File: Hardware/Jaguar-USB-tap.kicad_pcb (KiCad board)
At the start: 2 copper layers, 40 x 70 mm, 24 parts, among them J1 DB15, P1 CONN_01X03, P2 USB_B, P3 CONN_01X05, U1 NCP1117ST33T3G, U2 STM32F070F6, U3 TXB0106, U4 TXB0106, Y1 8MHz

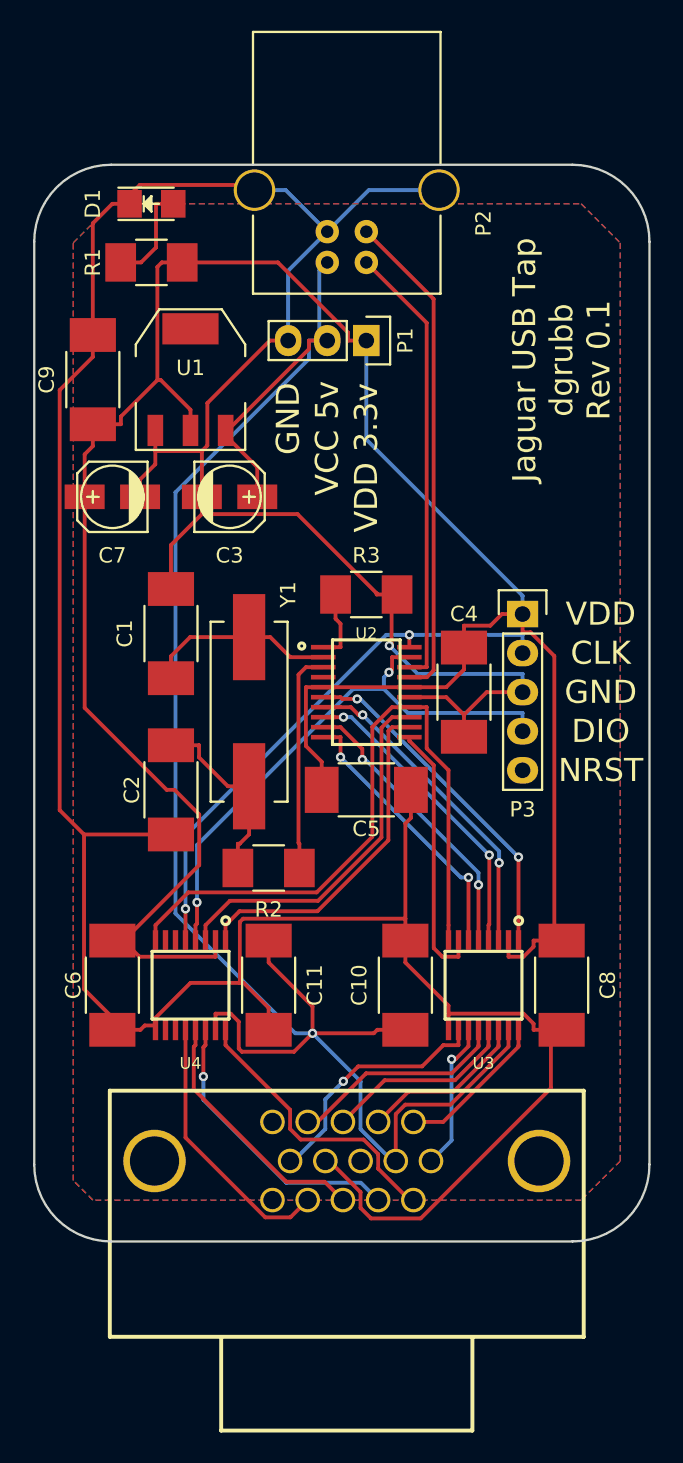
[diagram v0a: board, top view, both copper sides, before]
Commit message: Circuit improvements.
1) Add an indicator LED to OE.
2) Add a capacitor to NRST.
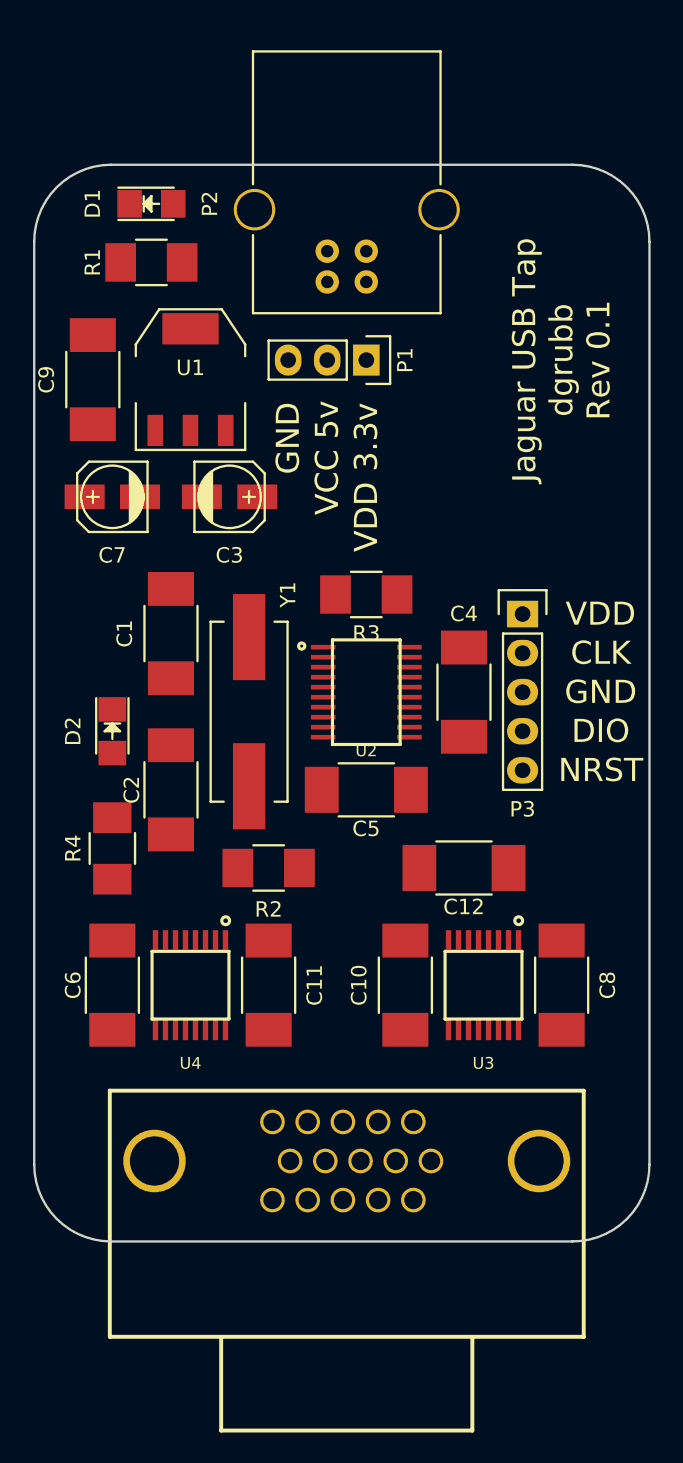
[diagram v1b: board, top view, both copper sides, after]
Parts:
- added C12: 0.1uF, Capacitors_SMD:C_1812_HandSoldering, F.Cu at (144.8, 90.2)
- added D2: LED, LEDs:LED_1206, F.Cu at (121.9, 81.3)
- added R4: 650, Resistors_SMD:R_1210_HandSoldering, F.Cu at (121.9, 88.9)
- moved P2 1.27 mm to (135.9, 52.1)
- moved P1 1.27 mm to (138.4, 57.1)
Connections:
- U2 pad 5: VDD -> NRST
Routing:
- net GNDREF: track 239.8 -> 0.00 mm, vias 1 -> 0
- net VDD: track 155.2 -> 0.00 mm
- net VCC: track 121.1 -> 0.00 mm, vias 1 -> 0
- net OE: track 44.5 -> 0.00 mm
- net R5_VDD: track 36.9 -> 0.00 mm, vias 2 -> 0
- net R6_VDD: track 36.2 -> 0.00 mm, vias 2 -> 0
- net D-: track 32.1 -> 0.00 mm
- net D+: track 29.1 -> 0.00 mm
- net R4_VDD: track 24.1 -> 0.00 mm
- net R3_VDD: track 22.5 -> 0.00 mm
- net C1_VDD: track 22.5 -> 0.00 mm, vias 2 -> 0
- net C2_VDD: track 21.2 -> 0.00 mm, vias 2 -> 0
- net C3_VDD: track 20.1 -> 0.00 mm, vias 2 -> 0
- net C4_VDD: track 18.9 -> 0.00 mm, vias 2 -> 0
- net R4_VCC: track 18.7 -> 0.00 mm, vias 1 -> 0
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- removed copper zone on B.Cu, net GNDREF
- removed copper zone on F.Cu, net VDD

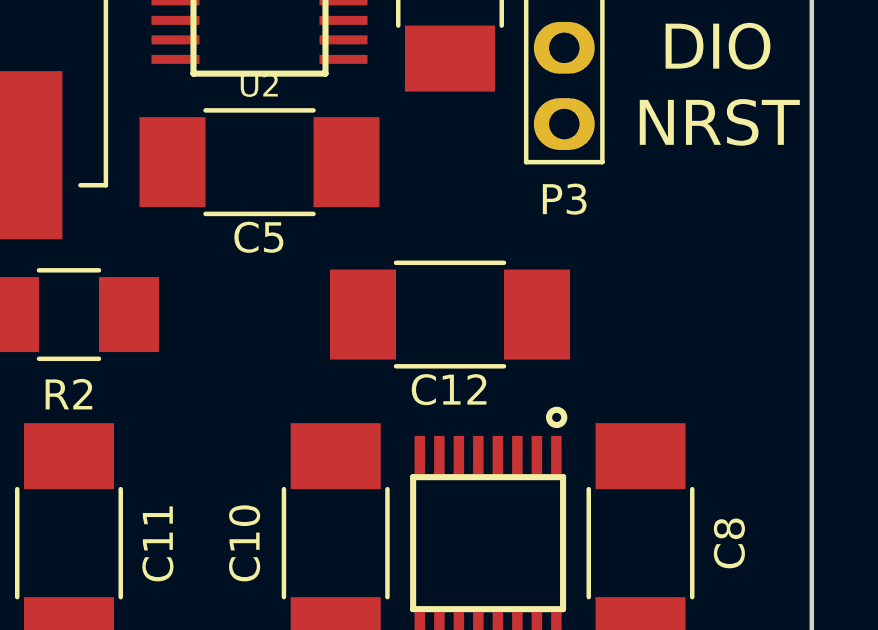
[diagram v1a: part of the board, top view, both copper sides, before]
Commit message: Minor tweaks for PCB layout positioning of components.
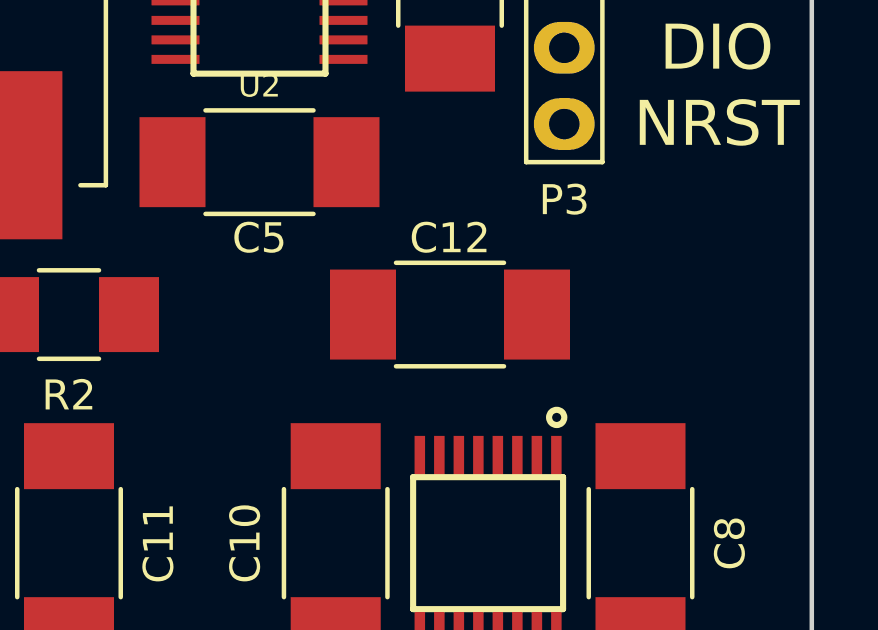
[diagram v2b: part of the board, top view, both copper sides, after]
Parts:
- turned C12 to 180 degrees
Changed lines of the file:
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@@
   )
   (module Capacitors_SMD:C_1812_HandSoldering (layer F.Cu)
-    (at 144.78 90.17)
+    (at 144.78 90.17 180)
     (descr "Capacitor SMD 1812, hand soldering")
     (tags "capacitor 1812")
     (attr smd)
-    (fp_text reference C12 (at 0 2.54) (layer F.SilkS)
+    (fp_text reference C12 (at 0 2.54 180) (layer F.SilkS)
       (effects (font (size 1 1) (thickness 0.15)))
     )
-    (fp_text value 0.1uF (at 0 3) (layer F.Fab)
+    (fp_text value 0.1uF (at 0 3 180) (layer F.Fab)
       (effects (font (size 1 1) (thickness 0.15)))
     )
@@
     (fp_line (start 1.8 -1.725) (end -1.8 -1.725) (layer F.SilkS) (width 0.15))
     (fp_line (start -1.8 1.725) (end 1.8 1.725) (layer F.SilkS) (width 0.15))
-    (pad 1 smd rect (at -2.9 0) (size 2.2 3) (layers F.Cu F.Paste F.Mask)
+    (pad 1 smd rect (at -2.9 0 180) (size 2.2 3) (layers F.Cu F.Paste F.Mask)
       (net 24 NRST))
-    (pad 2 smd rect (at 2.9 0) (size 2.2 3) (layers F.Cu F.Paste F.Mask)
+    (pad 2 smd rect (at 2.9 0 180) (size 2.2 3) (layers F.Cu F.Paste F.Mask)
       (net 2 GNDREF))
     (model Capacitors_SMD.3dshapes/C_1812_HandSoldering.wrl

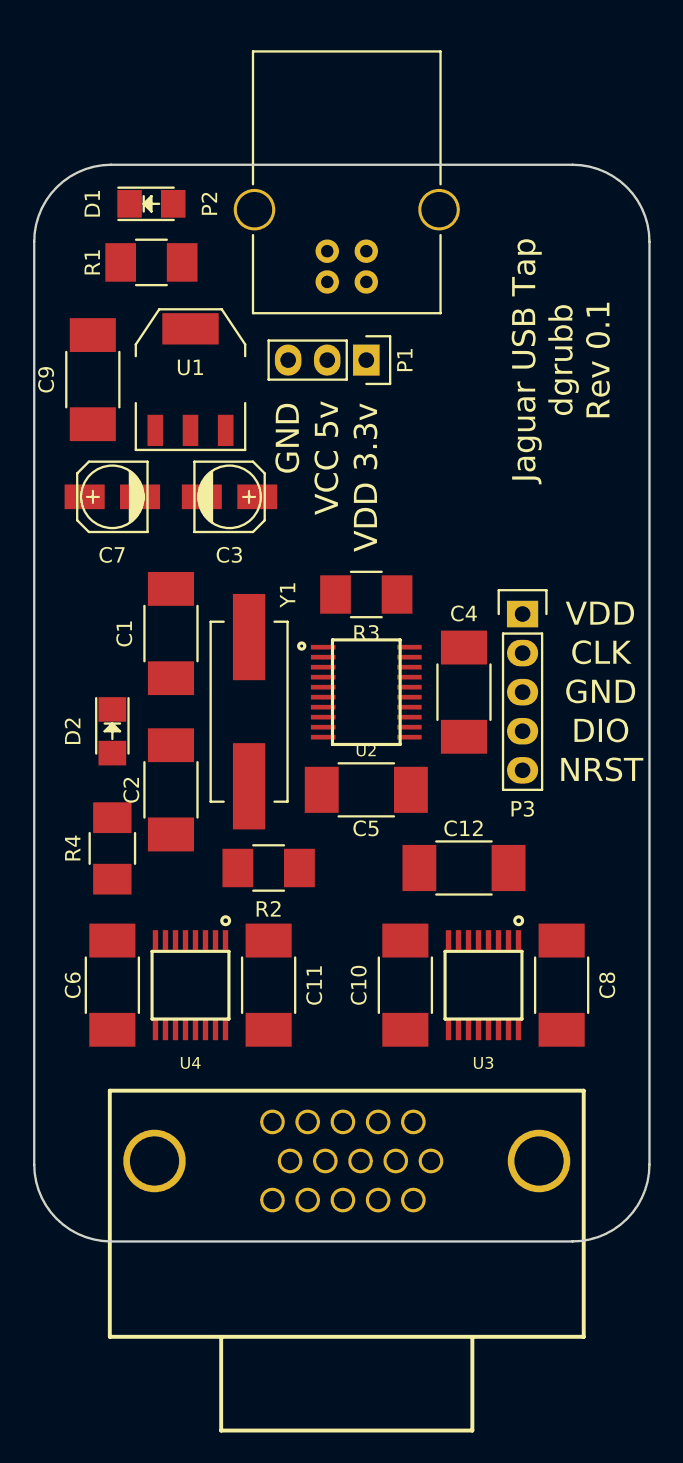
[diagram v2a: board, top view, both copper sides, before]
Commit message: Update Gerbers and drill files to reflect tweaks to schematic.
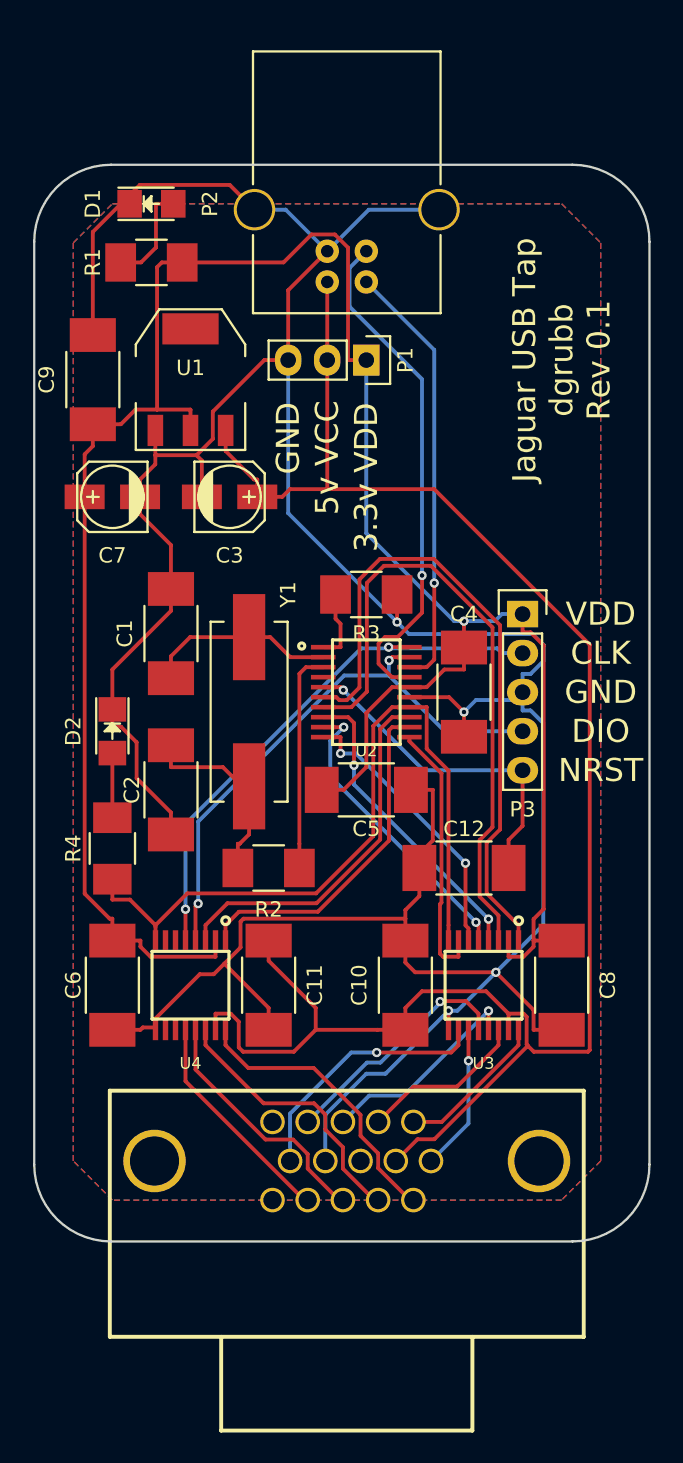
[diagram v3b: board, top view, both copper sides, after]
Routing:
- net GNDREF: track 0.00 -> 228.3 mm, vias 0 -> 4
- net VDD: track 0.00 -> 151.7 mm, vias 0 -> 1
- net VCC: track 0.00 -> 123.5 mm
- net OE: track 0.00 -> 49.3 mm
- net C1_VDD: track 0.00 -> 43.0 mm
- net C2_VDD: track 0.00 -> 41.9 mm
- net R5_VDD: track 0.00 -> 36.8 mm, vias 0 -> 2
- net R6_VDD: track 0.00 -> 35.8 mm, vias 0 -> 2
- net D-: track 0.00 -> 33.2 mm, vias 0 -> 1
- net D+: track 0.00 -> 28.2 mm, vias 0 -> 1
- net R4_VDD: track 0.00 -> 24.1 mm
- net R3_VDD: track 0.00 -> 22.5 mm
- net NRST: track 0.00 -> 21.9 mm, vias 0 -> 1
- net C3_VDD: track 0.00 -> 20.0 mm, vias 0 -> 2
- net C4_VDD: track 0.00 -> 19.6 mm, vias 0 -> 2
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- added copper zone on B.Cu, net GNDREF
- added copper zone on F.Cu, net VDD
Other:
- board text added: "3.3v VDD"
- board text added: "5v VCC"
- board text removed: "VCC 5v"
- board text removed: "VDD 3.3v"

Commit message: Update silkscreen artwork.
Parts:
- added G***: LOGO, SilkArt:Atari-Fuji-2cmx2cm, B.Cu at (129.5, 66.0)
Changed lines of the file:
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@@
 (kicad_pcb (version 4) (host pcbnew 4.0.2+dfsg1-stable)
   (general
-    (links 81)
+    (links 0)
     (no_connects 0)
     (area 116.764999 44.374999 156.915001 114.525001)
@@
     (tracks 423)
     (zones 0)
-    (modules 27)
+    (modules 28)
     (nets 41)
   )
   (page A4)
   (layers
-    (0 F.Cu signal)
-    (31 B.Cu signal)
+    (0 F.Cu signal hide)
+    (31 B.Cu signal hide)
     (32 B.Adhes user)
     (33 F.Adhes user)
@@
     )
   )
-  (gr_text "Jaguar USB Tap\ndgrubb\nRev 0.1" (at 151.13 57.15 90) (layer F.SilkS)
-    (effects (font (size 1.5 1.5) (thickness 0.3)))
+  (module SilkArt:Atari-Fuji-2cmx2cm (layer B.Cu)
+    (at 129.54 66.04 90)
+    (fp_text reference G*** (at 0 0 90) (layer B.SilkS) hide
+      (effects (font (thickness 0.3)) (justify mirror))
+    )
+    (fp_text value LOGO (at 0.75 0 90) (layer B.SilkS) hide
+      (effects (font (thickness 0.3)) (justify mirror))
+    )
+    (fp_poly (pts (xy -1.800482 7.714231) (xy -1.596011 7.489988) (xy -1.479103 6.962978) (xy -1.425607 6.007796)
+      (xy -1.411372 4.499039) (xy -1.411111 4.097456) (xy -1.514614 1.405386) (xy -1.854009 -0.757812)
+      (xy -2.472621 -2.542035) (xy -3.413778 -4.097179) (xy -3.980697 -4.792538) (xy -5.492194 -6.203342)
+      (xy -7.194743 -7.117166) (xy -8.768841 -7.573608) (xy -9.510026 -7.69036) (xy -9.81508 -7.475602)
+      (xy -9.877407 -6.756351) (xy -9.877777 -6.581777) (xy -9.800777 -5.743099) (xy -9.43588 -5.274464)
+      (xy -8.582246 -4.91882) (xy -8.577145 -4.917136) (xy -7.622761 -4.429926) (xy -6.489098 -3.609761)
+      (xy -5.656809 -2.861305) (xy -4.2579 -1.09522) (xy -3.352047 0.949806) (xy -2.8968 3.393833)
+      (xy -2.822222 5.155789) (xy -2.805056 6.496086) (xy -2.726975 7.278389) (xy -2.5481 7.649947)
+      (xy -2.228557 7.758007) (xy -2.116666 7.761111) (xy -1.800482 7.714231)) (layer B.SilkS) (width 0.01))
+    (fp_poly (pts (xy 1.411111 -7.761111) (xy -1.058333 -7.761111) (xy -1.058333 7.761111) (xy 1.411111 7.761111)
+      (xy 1.411111 -7.761111)) (layer B.SilkS) (width 0.01))
+    (fp_poly (pts (xy 2.706081 7.702375) (xy 2.924086 7.440612) (xy 3.066976 6.847493) (xy 3.167147 5.79469)
+      (xy 3.24885 4.321528) (xy 3.398219 2.328584) (xy 3.641988 0.860342) (xy 4.013181 -0.261377)
+      (xy 4.152413 -0.553231) (xy 5.179566 -2.070339) (xy 6.562149 -3.464185) (xy 8.072856 -4.52823)
+      (xy 8.969546 -4.930213) (xy 9.816123 -5.276156) (xy 10.153938 -5.700379) (xy 10.163454 -6.432083)
+      (xy 10.162184 -6.444927) (xy 10.005092 -7.233626) (xy 9.625797 -7.574898) (xy 8.851748 -7.551976)
+      (xy 8.166517 -7.407562) (xy 6.490902 -6.703911) (xy 4.862172 -5.465132) (xy 3.468599 -3.847344)
+      (xy 3.029977 -3.148235) (xy 2.583721 -2.316445) (xy 2.276325 -1.572187) (xy 2.076099 -0.747711)
+      (xy 1.951356 0.324735) (xy 1.870408 1.812899) (xy 1.82095 3.25211) (xy 1.768828 5.104528)
+      (xy 1.75807 6.365341) (xy 1.802752 7.147972) (xy 1.91695 7.565843) (xy 2.114743 7.732377)
+      (xy 2.380566 7.761111) (xy 2.706081 7.702375)) (layer B.SilkS) (width 0.01))
+  )
+  (gr_text "Jaguar USB Tap\ndgrubb\nRev 0.1" (at 129.54 82.55 270) (layer B.SilkS)
+    (effects (font (size 1.5 1.5) (thickness 0.3)) (justify mirror))
   )
   (gr_text "3.3v VDD" (at 138.43 64.77 90) (layer F.SilkS)
